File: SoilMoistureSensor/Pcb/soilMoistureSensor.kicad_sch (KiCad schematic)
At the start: 51 parts, among them J1 USB_B_Micro, J2 Conn_01x03, J3 Conn_01x02, J4 Conn_01x03, J5 Conn_01x03, U1 W25Q16JVUXIQ, U2 RP2040, U3 AP63357Q, Y1 12Mhz

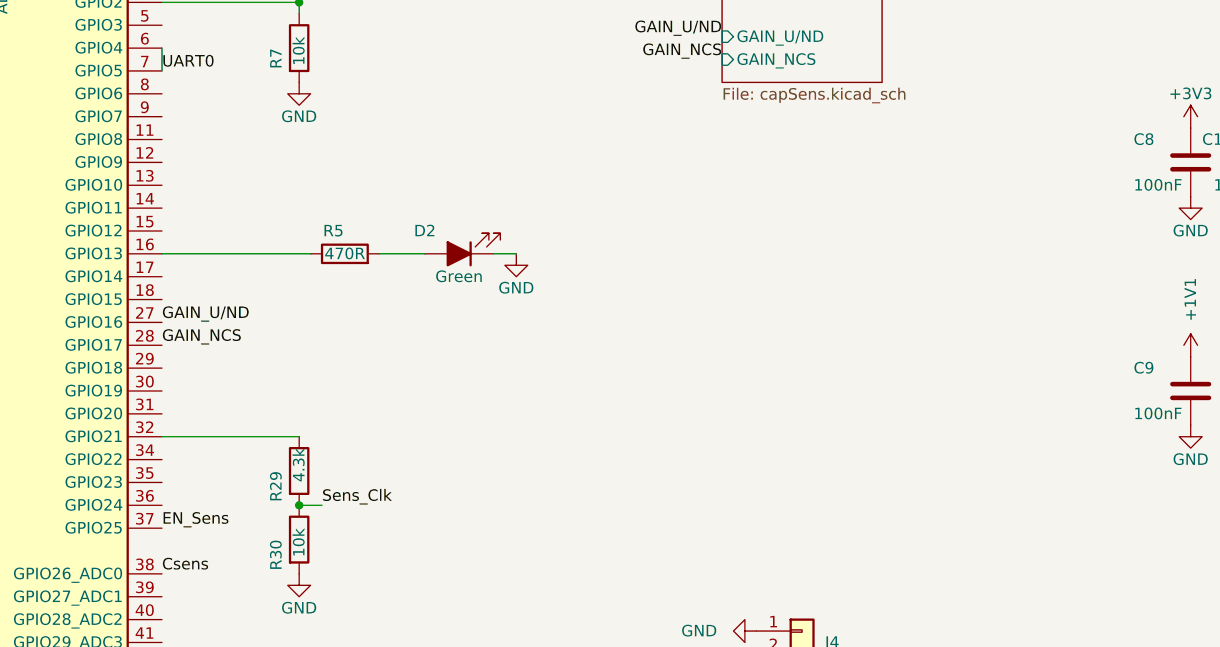
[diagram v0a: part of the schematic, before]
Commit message: added fluidsensor
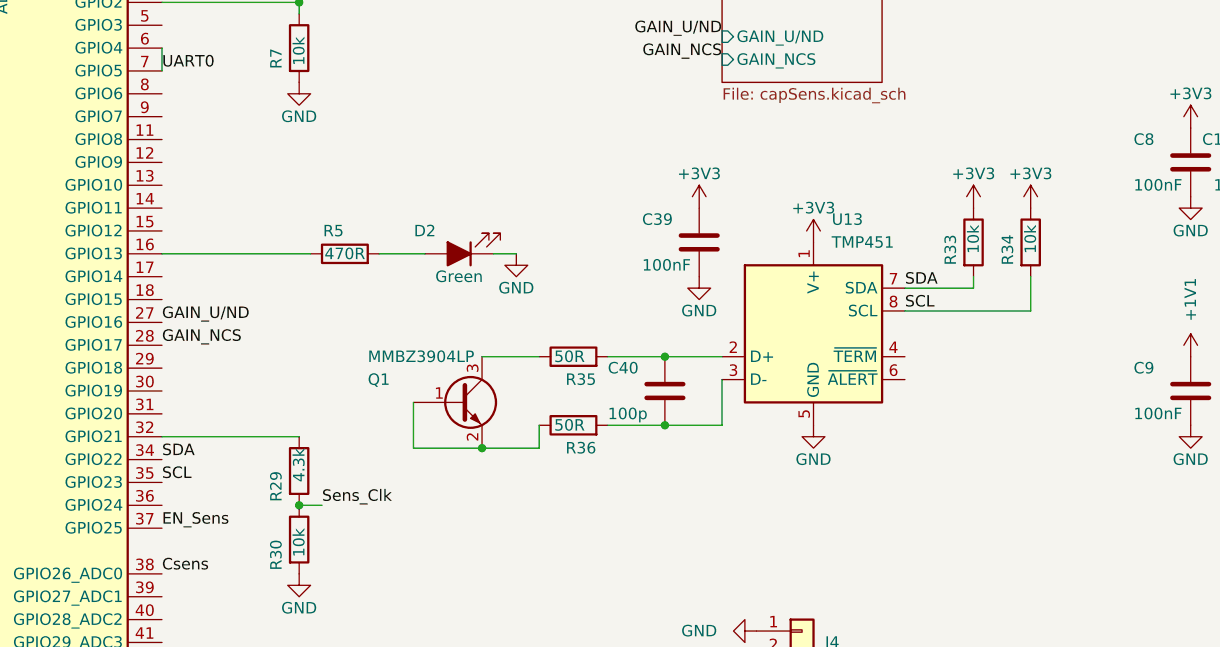
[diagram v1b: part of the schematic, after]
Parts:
- added C39: 100nF, Capacitor_SMD:C_0603_1608Metric, symbol Device:C
- added C40: 100p, Capacitor_SMD:C_0603_1608Metric, symbol Device:C
- added Q1: MMBZ3904LP, Package_DFN_QFN:Diodes_DFN1006-3, symbol Device:Q_NPN_BEC
- added R33, R34: 10k, Resistor_SMD:R_0603_1608Metric, symbol Device:R
- added R35, R36: 50R, Resistor_SMD:R_0603_1608Metric, symbol Device:R
- added U13: TMP451, Bergi:TI_WSON8_2x2mm_noEP, symbol Sensor_Temperature:TMP411
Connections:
- net +3V3: now also C39.1, R33.1, R34.1, U13.1 (V+)
- net GND: now also C39.2, U13.5 (GND)
- net SDA: now reaches U2.34 (GPIO22)
- net SDA: now also R33.2, U13.7 (SDA)
- net SCL: now reaches U2.35 (GPIO23)
- net SCL: now also R34.2, U13.8 (SCL)
- new net: C40.1, R35.2, U13.2 (D+)
- new net: C40.2, R36.2, U13.3 (D-)
- new net: Q1.3 (C), R35.1
- new net: Q1.1 (B), Q1.2 (E), R36.1

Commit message: wip
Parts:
- Q1: value MMBZ3904LP -> MMBT3904LP
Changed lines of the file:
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@@
       (effects (font (size 1.27 1.27)) (justify left))
     )
-    (property "Value" "MMBZ3904LP" (id 1) (at 128.27 110.49 0)
+    (property "Value" "MMBT3904LP" (id 1) (at 128.27 110.49 0)
       (effects (font (size 1.27 1.27)) (justify left))
     )
@@
     )
     (path "/cbffc1e8-9877-44a2-a34a-37ff86214e49"
-      (reference "Q1") (unit 1) (value "MMBZ3904LP") (footprint "Package_DFN_QFN:Diodes_DFN1006-3")
+      (reference "Q1") (unit 1) (value "MMBT3904LP") (footprint "Package_DFN_QFN:Diodes_DFN1006-3")
     )
     (path "/a9bd6db7-101e-488d-b0d8-6ad60600008c"

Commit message: wip
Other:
- note added: "Adr: 0x4C"
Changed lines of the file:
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@@
     (stroke (width 0) (type default) (color 0 0 0 0))
+  )
+  (text "Adr: 0x4C" (at 190.5 120.65 0)
+    (effects (font (size 1.27 1.27)) (justify left bottom))
   )
   (label "GAIN_U{slash}ND" (at 105.41 106.68 0)

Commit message: wip
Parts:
- U13: HTN (none) -> TMP451HQDQFRQ1
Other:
- note added: "Adr: 0x49"
- note removed: "Adr: 0x4C"
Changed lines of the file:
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@@
     (stroke (width 0) (type default) (color 0 0 0 0))
   )
-  (text "Adr: 0x4C" (at 190.5 120.65 0)
+  (text "Adr: 0x49" (at 190.5 120.65 0)
     (effects (font (size 1.27 1.27)) (justify left bottom))
   )
@@
       (effects (font (size 1.27 1.27)) hide)
     )
+    (property "HTN" "TMP451HQDQFRQ1" (id 4) (at 177.8 107.95 0)
+      (effects (font (size 1.27 1.27)) hide)
+    )
